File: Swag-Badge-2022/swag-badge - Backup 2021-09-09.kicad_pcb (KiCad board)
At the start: 2 copper layers, 132.8 x 135 mm, 11 parts, among them J7 Lolin32, P1 SAO_1, P2 SAO_2+ SPI, P3 SAO_3 + SPI, SW1 RESET, T3 Touch_Slider_Left, T4 Touch_Slider_Right

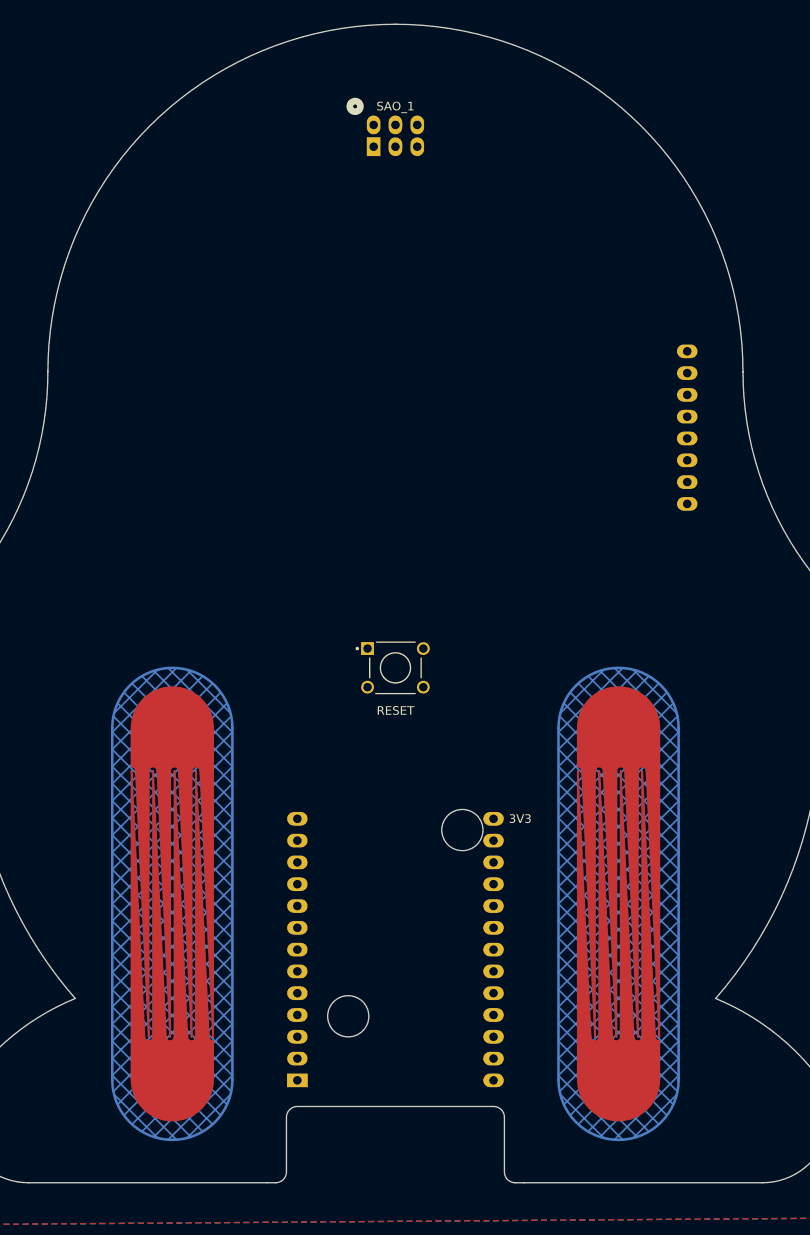
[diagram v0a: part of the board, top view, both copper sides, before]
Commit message: Schematic edited - Screen
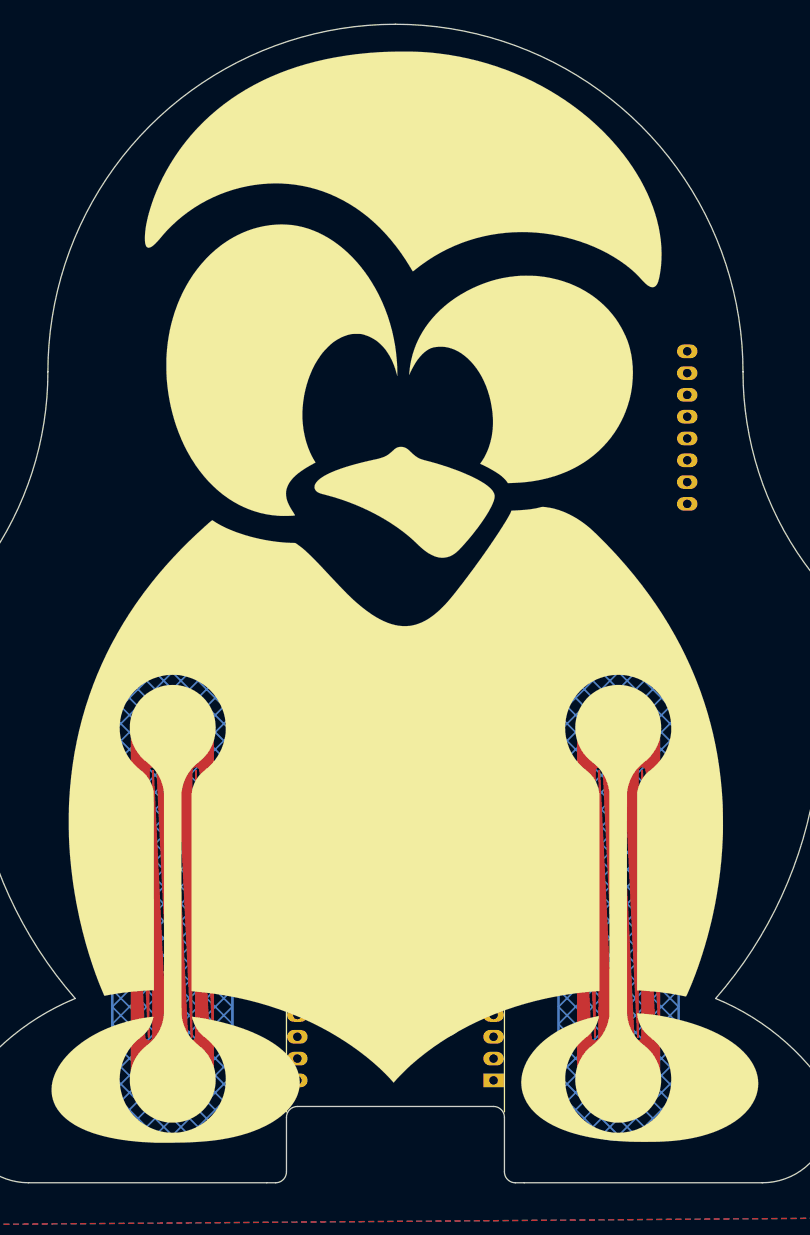
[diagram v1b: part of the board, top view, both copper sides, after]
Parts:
- added Ref**: Val**, SwagBadge:Logo_LCA_2022_01, B.Cu at (0.11, -168.7)
- added Ref**: Val**, SwagBadge:Tux_Silk_With_Slider_135, F.Cu at (0.05, -167.2)
- added Ref**: Val**, SwagBadge:SwagBadge_Logo_2022_Invert, B.Cu at (-0.01, -197.5)
- added Ref**: Val**, SwagBadge:QR_Code_OHMC2022_15mm, B.Cu at (-26.0, -198.2)
- J7: moved to F.Cu
- moved L3 1.34 mm to (40.5, -109.0)
- turned J7 to 0 degrees
